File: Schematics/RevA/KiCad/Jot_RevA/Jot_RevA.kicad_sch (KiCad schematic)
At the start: 0 parts

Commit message: KiCad: fill in schematic title block
Co-Authored-By: Claude Opus 5.5 <noreply@anthropic.com>
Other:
- company: (none) -> James Donal Cronin
- title: (none) -> Jot Rev A
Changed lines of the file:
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@@
 	(generator_version "10.0")
 	(paper "A4")
+	(title_block
+		(title "Jot Rev A")
+		(date "2026-10-02")
+		(rev "A")
+		(company "James Donal Cronin")
+		(comment 1 "JOT-HW-001: handheld push-to-talk voice capture")
+	)
 	(sheet_instances
 		(path "/"

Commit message: KiCad: add Power hierarchical sheet
Co-Authored-By: Claude Opus 5.5 <noreply@anthropic.com>
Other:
- added sheet Power (Power.kicad_sch)
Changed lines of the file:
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@@
 		(comment 1 "JOT-HW-001: handheld push-to-talk voice capture")
+	)
+	(sheet
+		(at 13.97 13.97)
+		(size 82.55 68.58)
+		(exclude_from_sim no)
+		(in_bom yes)
+		(on_board yes)
+		(dnp no)
+		(fields_autoplaced yes)
+		(stroke
+			(width 0.1524)
+			(type solid)
+		)
+		(fill
+			(color 0 0 0 0)
+		)
+		(property "Sheetname" "Power"
+			(at 13.97 13.2584 0)
+			(show_name no)
+			(do_not_autoplace no)
+			(effects
+				(font
+					(size 1.27 1.27)
+				)
+				(justify left bottom)
+			)
+		)
+		(property "Sheetfile" "Power.kicad_sch"
+			(at 13.97 83.1346 0)
+			(show_name no)
+			(do_not_autoplace no)
+			(effects
+				(font
+					(size 1.27 1.27)
+				)
+				(justify left top)
+			)
+		)
+		(instances
+			(project "Jot_RevA"
+				(path "/61747270-9f90-47b6-9c50-5ea1f41f259a"
+					(page "2")
+				)
+			)
+		)
 	)
 	(sheet_instances

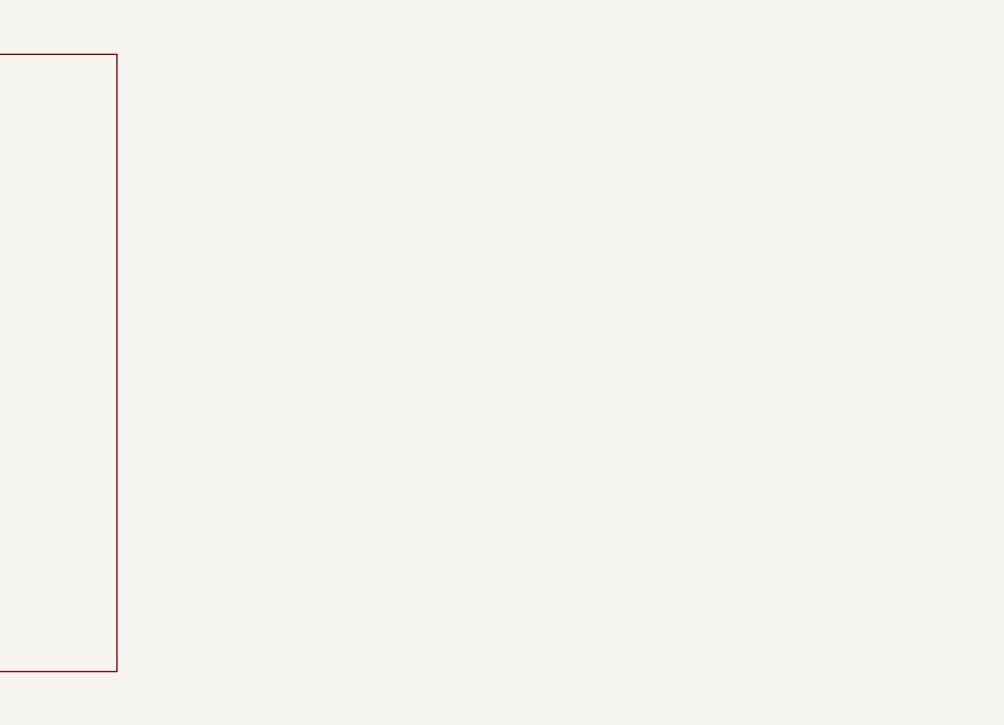
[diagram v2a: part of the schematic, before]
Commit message: KiCad: add MCU hierarchical sheet
Co-Authored-By: Claude Opus 5.5 <noreply@anthropic.com>
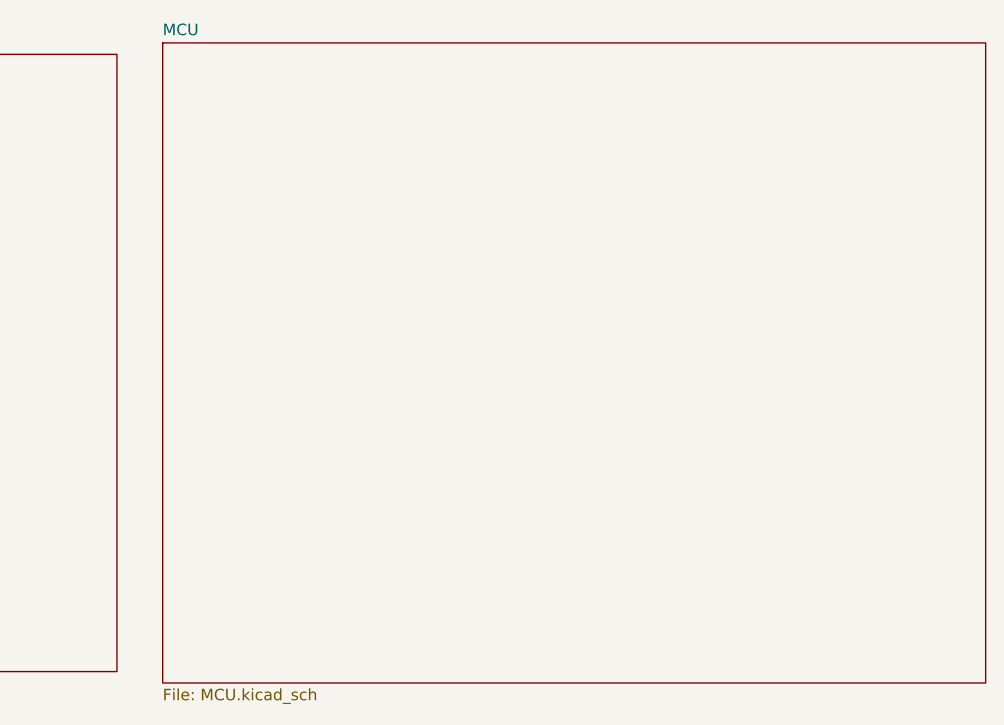
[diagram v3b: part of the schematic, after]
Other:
- added sheet MCU (MCU.kicad_sch)
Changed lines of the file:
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@@
+	)
+	(sheet
+		(at 101.6 12.7)
+		(size 91.44 71.12)
+		(exclude_from_sim no)
+		(in_bom yes)
+		(on_board yes)
+		(dnp no)
+		(fields_autoplaced yes)
+		(stroke
+			(width 0.1524)
+			(type solid)
+		)
+		(fill
+			(color 0 0 0 0)
+		)
+		(property "Sheetname" "MCU"
+			(at 101.6 11.9884 0)
+			(show_name no)
+			(do_not_autoplace no)
+			(effects
+				(font
+					(size 1.27 1.27)
+				)
+				(justify left bottom)
+			)
+		)
+		(property "Sheetfile" "MCU.kicad_sch"
+			(at 101.6 84.4046 0)
+			(show_name no)
+			(do_not_autoplace no)
+			(effects
+				(font
+					(size 1.27 1.27)
+				)
+				(justify left top)
+			)
+		)
+		(instances
+			(project "Jot_RevA"
+				(path "/61747270-9f90-47b6-9c50-5ea1f41f259a"
+					(page "3")
+				)
+			)
+		)
 	)
 	(sheet

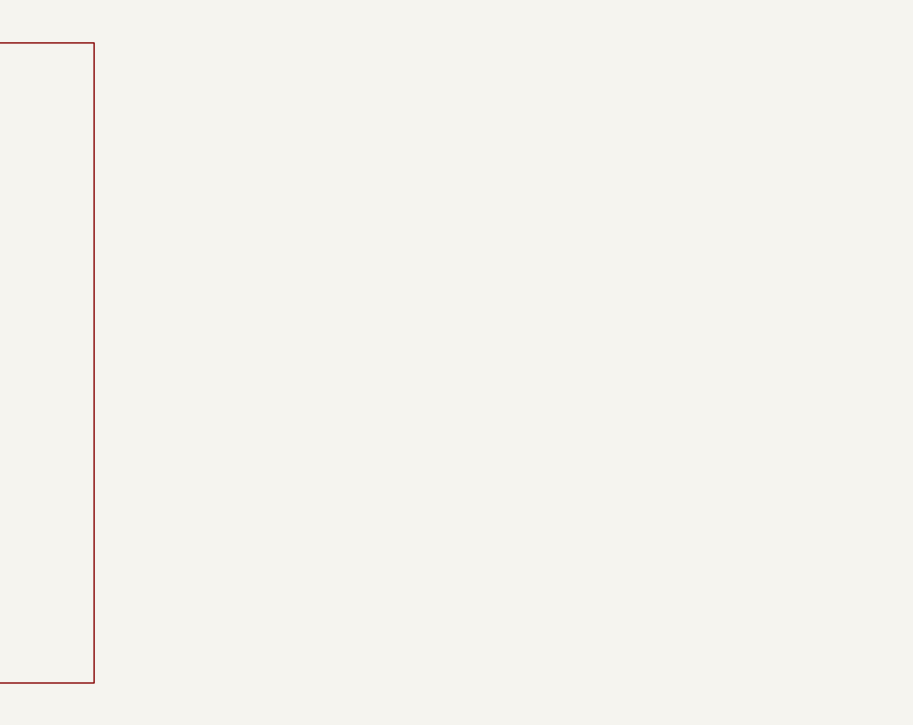
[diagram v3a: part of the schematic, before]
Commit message: Rev A schematic: MCU sheet updates, new Storage sheet
Co-Authored-By: Claude Opus 5.5 <noreply@anthropic.com>
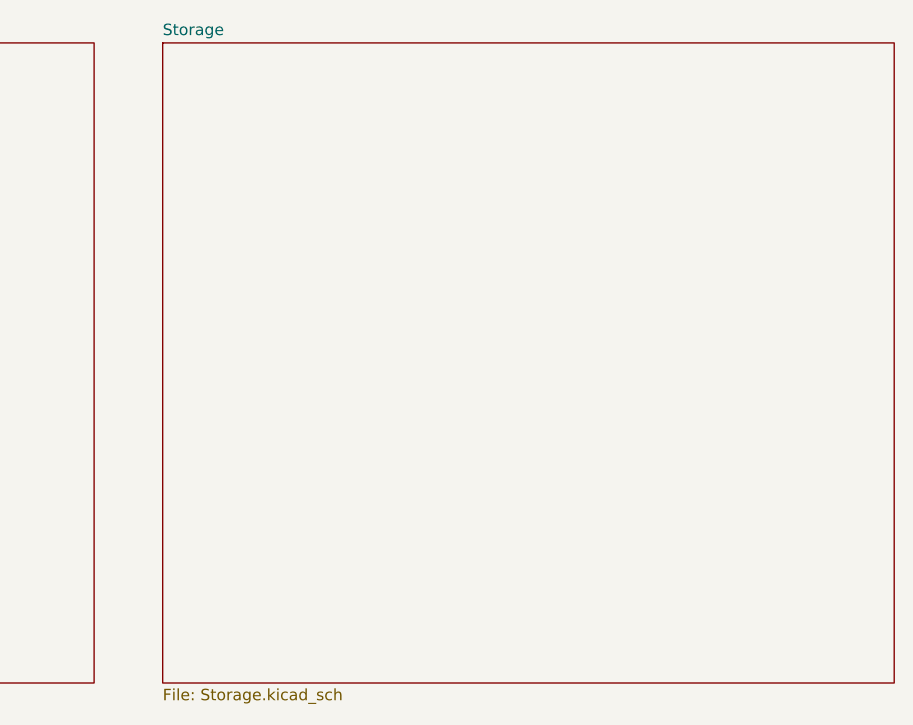
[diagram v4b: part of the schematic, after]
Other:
- added sheet Storage (Storage.kicad_sch)
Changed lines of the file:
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@@
+	)
+	(sheet
+		(at 200.66 12.7)
+		(size 81.28 71.12)
+		(exclude_from_sim no)
+		(in_bom yes)
+		(on_board yes)
+		(dnp no)
+		(fields_autoplaced yes)
+		(stroke
+			(width 0.1524)
+			(type solid)
+		)
+		(fill
+			(color 0 0 0 0)
+		)
+		(property "Sheetname" "Storage"
+			(at 200.66 11.9884 0)
+			(show_name no)
+			(do_not_autoplace no)
+			(effects
+				(font
+					(size 1.27 1.27)
+				)
+				(justify left bottom)
+			)
+		)
+		(property "Sheetfile" "Storage.kicad_sch"
+			(at 200.66 84.4046 0)
+			(show_name no)
+			(do_not_autoplace no)
+			(effects
+				(font
+					(size 1.27 1.27)
+				)
+				(justify left top)
+			)
+		)
+		(instances
+			(project "Jot_RevA"
+				(path "/61747270-9f90-47b6-9c50-5ea1f41f259a"
+					(page "4")
+				)
+			)
+		)
 	)
 	(sheet

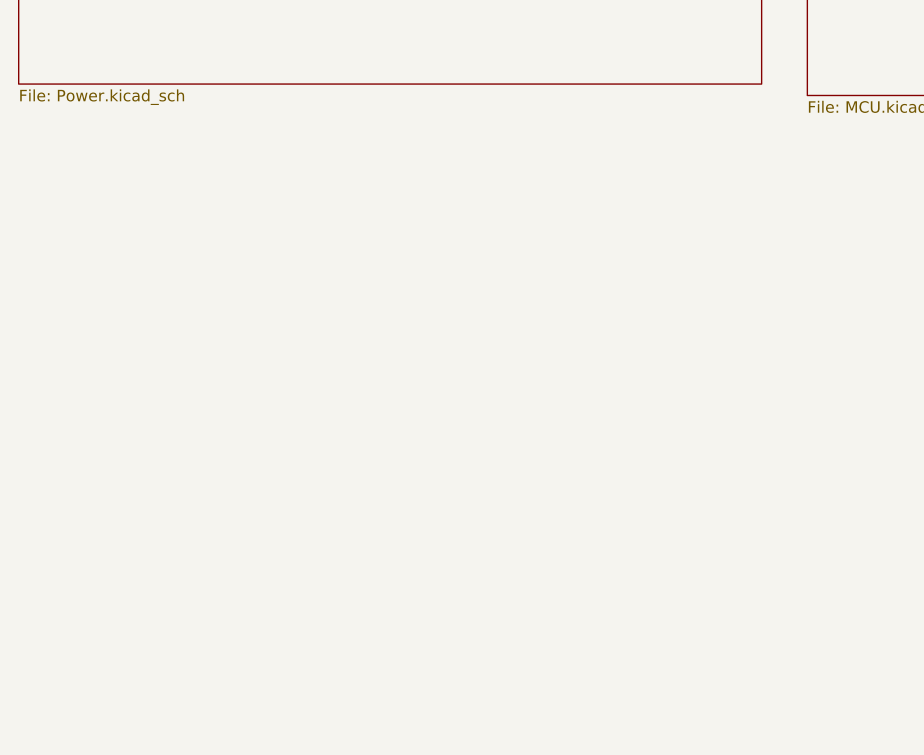
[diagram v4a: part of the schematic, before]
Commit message: Audio sheet: Q2 mic power switch with R13 pull-up, U2 T3902 mic, C11; flash back to U4
Co-Authored-By: Claude Opus 5.5 <noreply@anthropic.com>
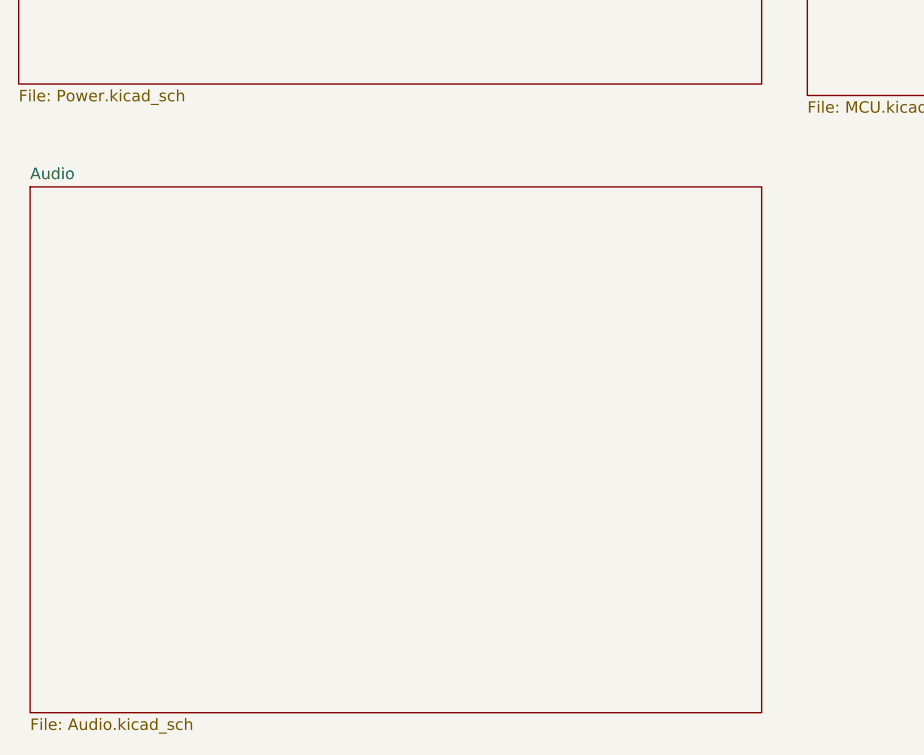
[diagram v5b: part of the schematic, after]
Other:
- added sheet Audio (Audio.kicad_sch)
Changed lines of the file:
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@@
+		)
+	)
+	(sheet
+		(at 15.24 93.98)
+		(size 81.28 58.42)
+		(exclude_from_sim no)
+		(in_bom yes)
+		(on_board yes)
+		(dnp no)
+		(fields_autoplaced yes)
+		(stroke
+			(width 0.1524)
+			(type solid)
+		)
+		(fill
+			(color 0 0 0 0)
+		)
+		(property "Sheetname" "Audio"
+			(at 15.24 93.2684 0)
+			(show_name no)
+			(do_not_autoplace no)
+			(effects
+				(font
+					(size 1.27 1.27)
+				)
+				(justify left bottom)
+			)
+		)
+		(property "Sheetfile" "Audio.kicad_sch"
+			(at 15.24 152.9846 0)
+			(show_name no)
+			(do_not_autoplace no)
+			(effects
+				(font
+					(size 1.27 1.27)
+				)
+				(justify left top)
+			)
+		)
+		(instances
+			(project "Jot_RevA"
+				(path "/61747270-9f90-47b6-9c50-5ea1f41f259a"
+					(page "5")
+				)
+			)
 		)
 	)

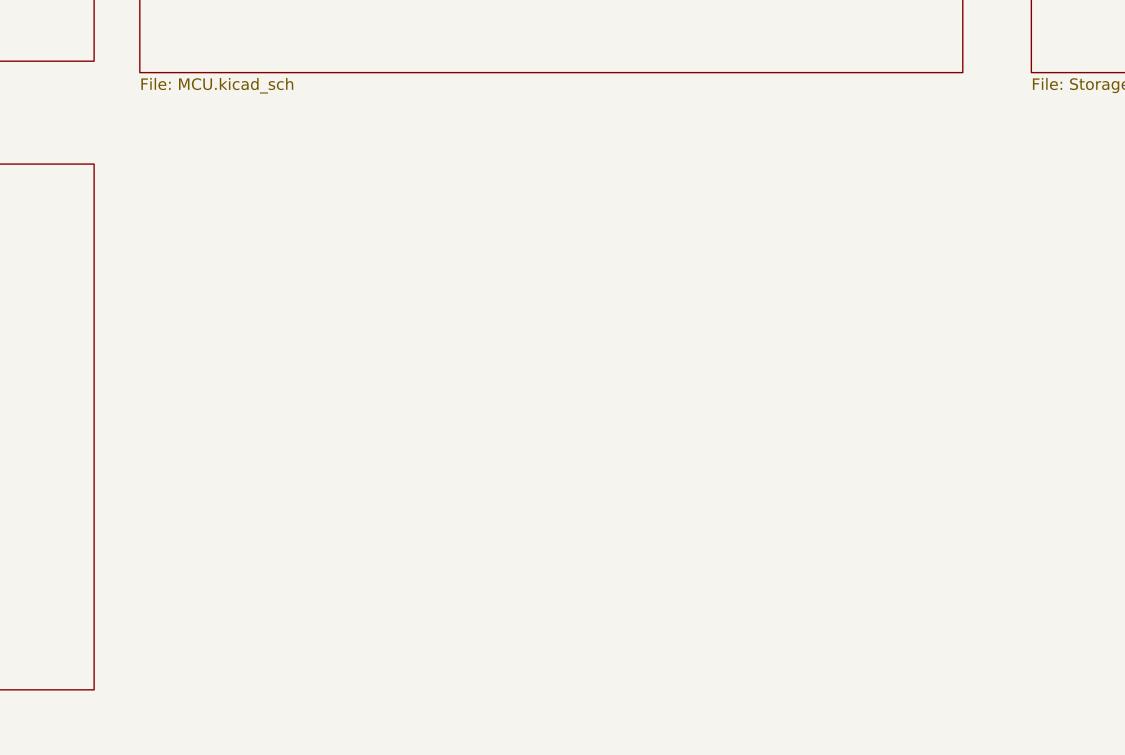
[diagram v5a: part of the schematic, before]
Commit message: Sensors sheet: new empty sheet linked from the top level, title block
Co-Authored-By: Claude Opus 5.5 <noreply@anthropic.com>
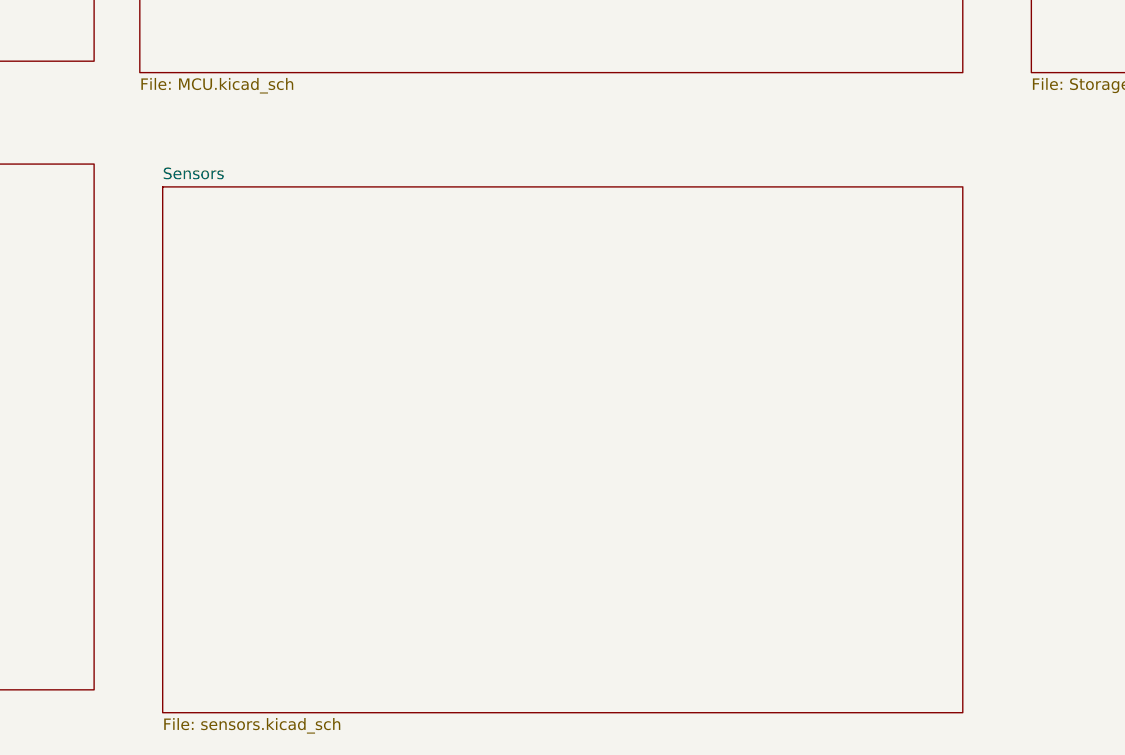
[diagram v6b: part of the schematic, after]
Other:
- added sheet Sensors (sensors.kicad_sch)
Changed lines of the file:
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@@
+	)
+	(sheet
+		(at 104.14 96.52)
+		(size 88.9 58.42)
+		(exclude_from_sim no)
+		(in_bom yes)
+		(on_board yes)
+		(dnp no)
+		(fields_autoplaced yes)
+		(stroke
+			(width 0.1524)
+			(type solid)
+		)
+		(fill
+			(color 0 0 0 0)
+		)
+		(property "Sheetname" "Sensors"
+			(at 104.14 95.8084 0)
+			(show_name no)
+			(do_not_autoplace no)
+			(effects
+				(font
+					(size 1.27 1.27)
+				)
+				(justify left bottom)
+			)
+		)
+		(property "Sheetfile" "sensors.kicad_sch"
+			(at 104.14 155.5246 0)
+			(show_name no)
+			(do_not_autoplace no)
+			(effects
+				(font
+					(size 1.27 1.27)
+				)
+				(justify left top)
+			)
+		)
+		(instances
+			(project "Jot_RevA"
+				(path "/61747270-9f90-47b6-9c50-5ea1f41f259a"
+					(page "6")
+				)
+			)
+		)
 	)
 	(sheet

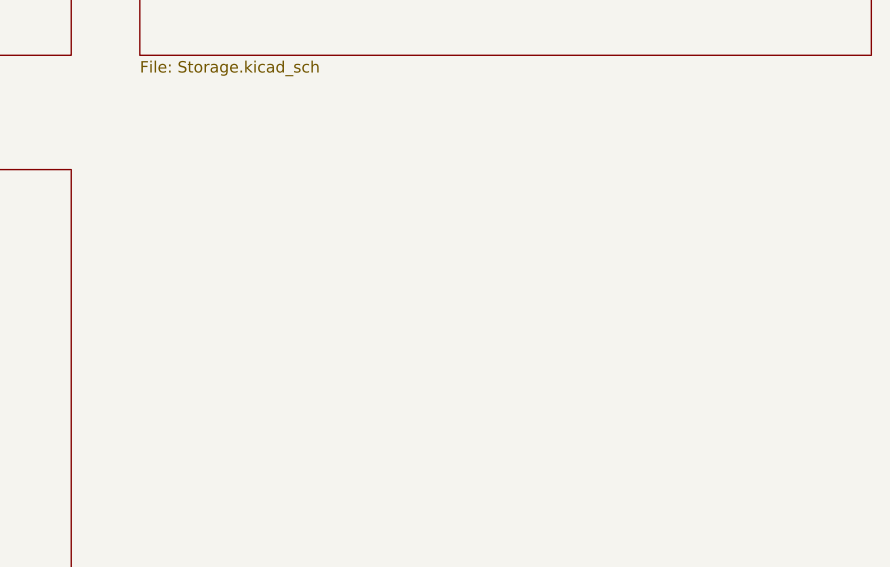
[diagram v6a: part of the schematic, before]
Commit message: UI sheet: new empty sheet linked from the top level
Co-Authored-By: Claude Opus 5.5 <noreply@anthropic.com>
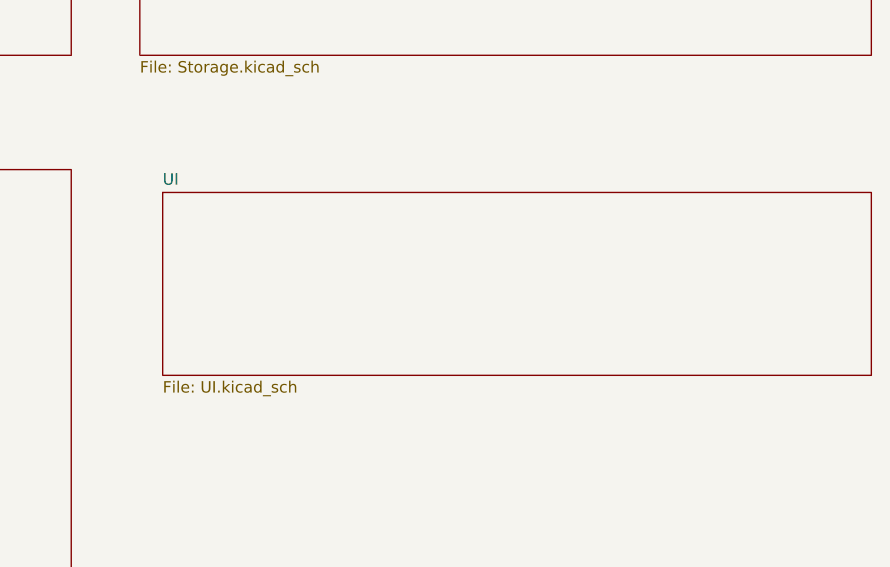
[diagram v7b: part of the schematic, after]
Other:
- added sheet UI (UI.kicad_sch)
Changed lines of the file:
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@@
+	)
+	(sheet
+		(at 203.2 99.06)
+		(size 78.74 20.32)
+		(exclude_from_sim no)
+		(in_bom yes)
+		(on_board yes)
+		(dnp no)
+		(fields_autoplaced yes)
+		(stroke
+			(width 0.1524)
+			(type solid)
+		)
+		(fill
+			(color 0 0 0 0)
+		)
+		(property "Sheetname" "UI"
+			(at 203.2 98.3484 0)
+			(show_name no)
+			(do_not_autoplace no)
+			(effects
+				(font
+					(size 1.27 1.27)
+				)
+				(justify left bottom)
+			)
+		)
+		(property "Sheetfile" "UI.kicad_sch"
+			(at 203.2 119.9646 0)
+			(show_name no)
+			(do_not_autoplace no)
+			(effects
+				(font
+					(size 1.27 1.27)
+				)
+				(justify left top)
+			)
+		)
+		(instances
+			(project "Jot_RevA"
+				(path "/61747270-9f90-47b6-9c50-5ea1f41f259a"
+					(page "7")
+				)
+			)
+		)
 	)
 	(sheet
